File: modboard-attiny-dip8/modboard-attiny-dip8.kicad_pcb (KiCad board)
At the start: 2 copper layers, 32.8 x 51.6 mm, 8 parts, among them J1 modboard-edge-connector, J2 Conn_01x03_Male, U1 ATTINY85-20PU, Y1 Crystal

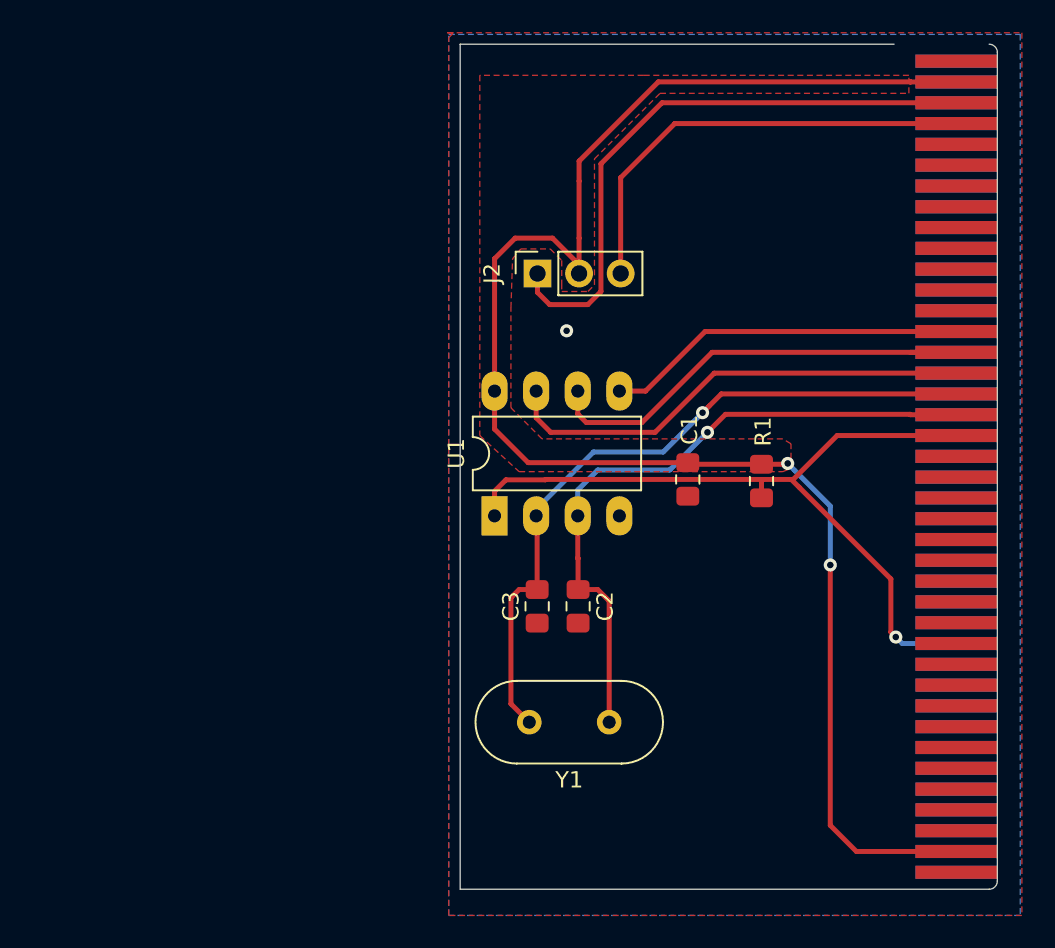
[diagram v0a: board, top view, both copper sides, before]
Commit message: Updated connector and board size
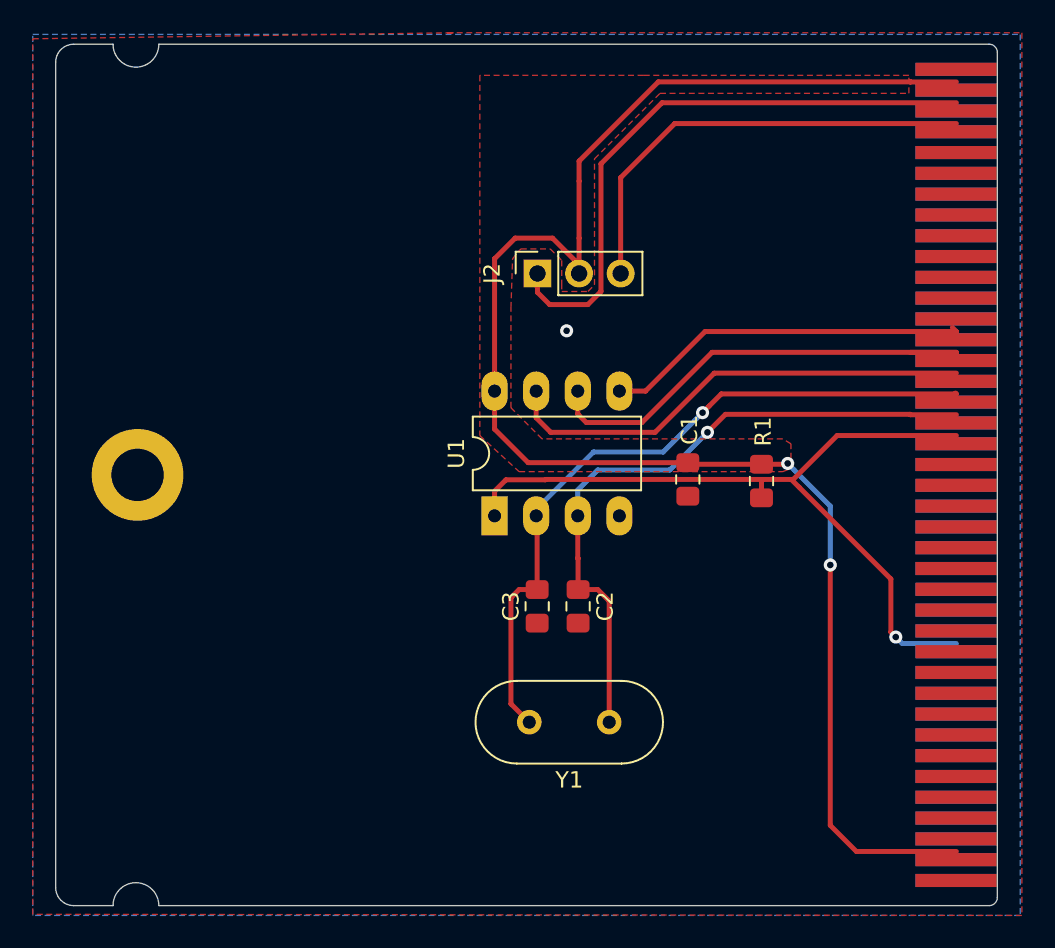
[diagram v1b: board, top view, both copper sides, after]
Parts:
- added REF**: MountingHole_3.2mm_M3_DIN965_Pad, MountingHole:MountingHole_3.2mm_M3_DIN965_Pad, F.Cu at (48.0, 86.8)
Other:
- board size 32.8 x 51.6 mm -> 57.5 x 52.6 mm

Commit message: Added ICP connections, labeled VBUS header
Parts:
- removed REF**: MountingHole_3.2mm_M3_DIN965_Pad, MountingHole:MountingHole_3.2mm_M3_DIN965_Pad
- J2: footprint Connector_PinSocket_2.54mm:PinSocket_1x03_P2.54mm_Vertical -> Connector_PinHeader_2.54mm:PinHeader_1x03_P2.54mm_Vertical
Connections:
- J1 pad 36: (no net) -> MOSI
- J1 pad 42: (no net) -> GND
- J1 pad 44: (no net) -> RESET
- J1 pad 46: (no net) -> GND
- J1 pad 48: (no net) -> SCK
- J1 pad 50: (no net) -> GND
- J1 pad 52: (no net) -> MISO
- J1 pad 54: (no net) -> GND
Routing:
- net MOSI: track 22.4 -> 31.7 mm
- net MISO: track 29.3 -> 35.8 mm, vias 0 -> 1
- net GND: vias 0 -> 9
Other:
- board text added: "3V3"
- board text added: "5V"

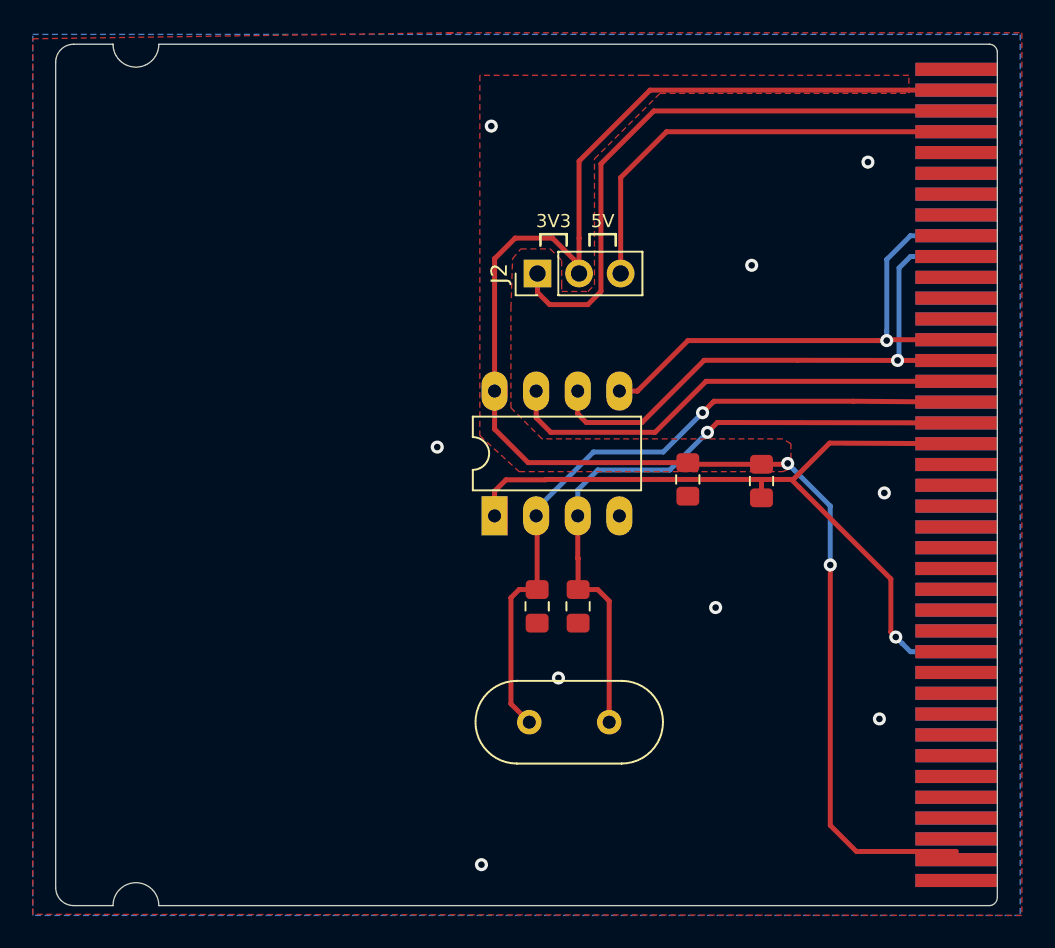
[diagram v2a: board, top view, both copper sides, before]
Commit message: Added mounting hole, fixed routing
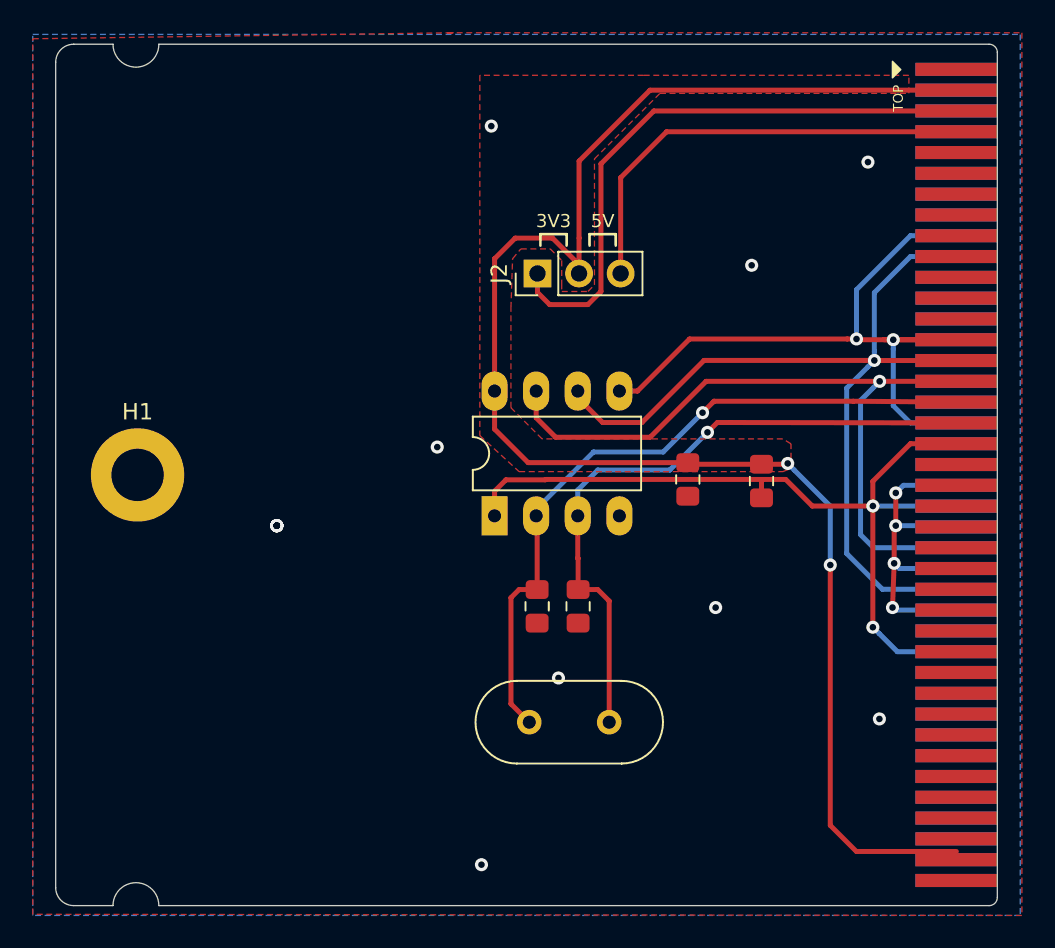
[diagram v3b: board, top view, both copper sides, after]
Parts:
- added ATTINY-DIP8: LOGO_BRD_REF, qboards_aesthetics:logo_url-5mm, B.Cu at (47.6, 65.2)
- added H1: MountingHole_Pad, MountingHole:MountingHole_3.2mm_M3_ISO7380_Pad, F.Cu at (48.0, 86.8)
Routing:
- net GND: track 0.00 -> 22.6 mm, vias 9 -> 17
- net MISO: track 35.8 -> 55.9 mm
- net SCK: track 29.3 -> 45.6 mm, vias 0 -> 1
- net MOSI: track 31.7 -> 45.1 mm, vias 1 -> 2
- net RESET: track 48.8 -> 52.9 mm, vias 1 -> 2
